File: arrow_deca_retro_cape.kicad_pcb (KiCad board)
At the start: 2 copper layers, 100 x 100 mm, 78 parts, among them J1 DB15_Female_HighDensity_Mount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, J10 Conn_02x06_Odd_Even, J11 PMOD1, J12 PMOD2, J14 Conn_01x02, J15 Conn_01x03, J16 Conn_01x06, J17 Conn_01x02, J18 Conn_01x03, J19 DINC_MIN_TM_6_1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

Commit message: v0.71 gerbers sent for manufacturing
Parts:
- C18: value 10uF -> 1uF
- C19, C21: value 100uF -> 10uF
- C20: value 10uF -> 0.1uF
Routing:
- net GND: track 51.3 -> 61.3 mm, vias 6 -> 7
- net +3V3: track 244.5 -> 253.2 mm, vias 2 -> 3
- net Net-(D5-Pad3): track 137.0 -> 139.6 mm
- net +5V: track 281.3 -> 280.2 mm
- net /MUX: track 84.1 -> 83.6 mm
- net /RX+: track 107.4 -> 107.9 mm
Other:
- board text added: "0.1270 mm / 0.1270 mm"
- board text added: "0.3000 mm"
- board text added: "1.6000 mm"
- board text removed: "0.1270 mm"
- board text removed: "0.1270 mm / 0.0000 mm"
- board text removed: "0.5700 mm"

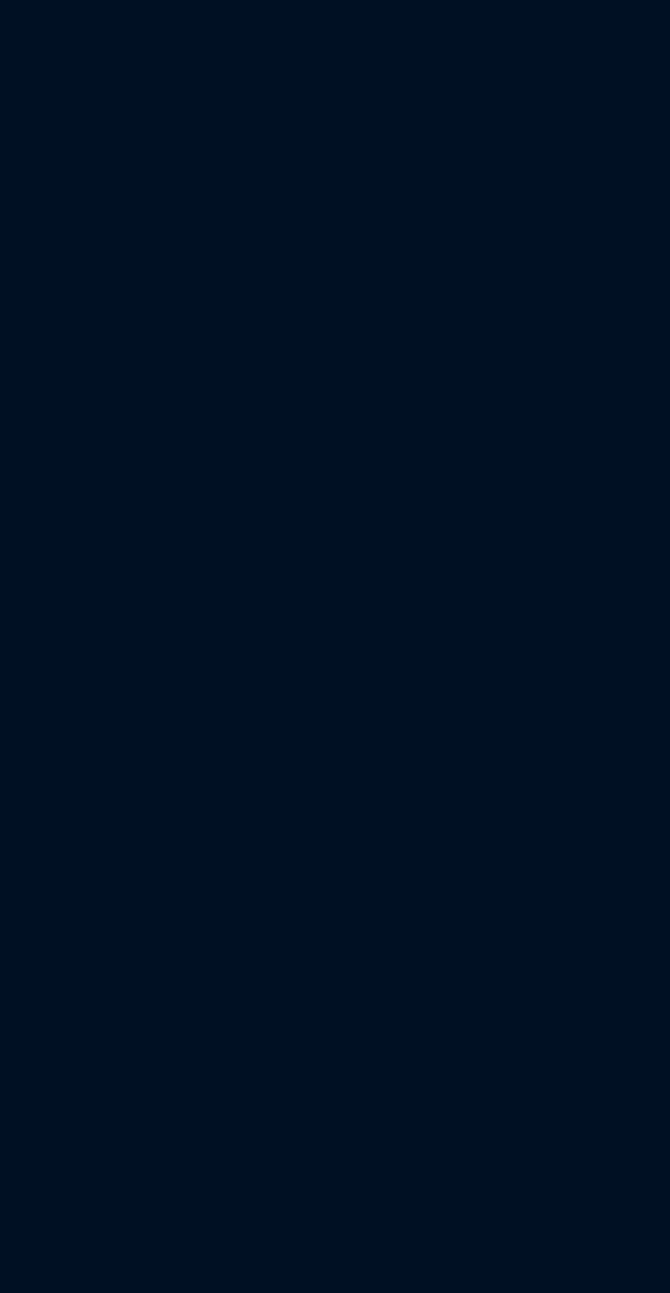
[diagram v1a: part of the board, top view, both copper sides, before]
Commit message: updated status. received pcb. started testing
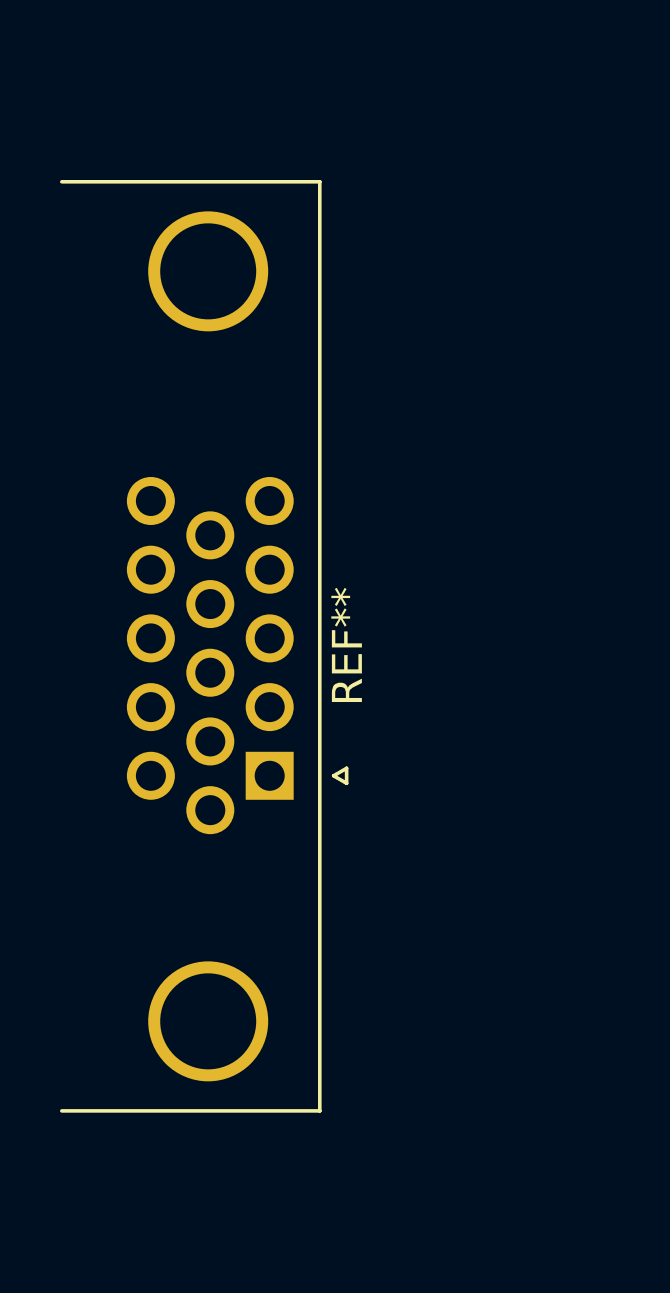
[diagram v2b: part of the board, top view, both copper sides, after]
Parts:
- added REF**: DSUB-15-HD_Female_Horizontal_P2.29x1.98mm_EdgePinOffset3.03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, Connector_Dsub:DSUB-15-HD_Female_Horizontal_P2.29x1.98mm_EdgePinOffset3.03mm_Housed_MountingHolesOffset4.94mm, F.Cu at (53.3, 64.4)
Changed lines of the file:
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@@
     )
   )
-  (property "VERSION" "0.71")
+  (property "VERSION" "0.72")
   (net 0 "")
   (net 1 "GND")
@@
       (offset (xyz 0 0 0))
       (scale (xyz 1 1 1))
+      (rotate (xyz 0 0 0))
+    )
+  )
+  (footprint "Connector_Dsub:DSUB-15-HD_Female_Horizontal_P2.29x1.98mm_EdgePinOffset3.03mm_Housed_MountingHolesOffset4.94mm" (layer "F.Cu")
+    (at 53.34 64.4386 -90)
+    (descr "15-pin D-Sub connector, horizontal/angled (90 deg), THT-mount, female, pitch 2.29x1.98mm, pin-PCB-offset 3.0300000000000002mm, distance of mounting holes 25mm, distance of mounting holes to PCB edge 4.9399999999999995mm, see https://disti-assets.s3.amazonaws.com/tonar/files/datasheets/16730.pdf")
+    (tags "15-pin D-Sub connector horizontal angled 90deg THT female pitch 2.29x1.98mm pin-PCB-offset 3.0300000000000002mm mounting-holes-distance 25mm mounting-hole-offset 25mm")
+    (attr through_hole)
+    (fp_text reference "REF**" (at -4.315 -2.61 90) (layer "F.SilkS")
+      (effects (font (size 1 1) (thickness 0.15)))
+    )
+    (fp_text value "DSUB-15-HD_Female_Horizontal_P2.29x1.98mm_EdgePinOffset3.03mm_Housed_MountingHolesOffset4.94mm" (at -4.315 14.89 90) (layer "F.Fab")
+      (effects (font (size 1 1) (thickness 0.15)))
+    )
+    (fp_text user "${REFERENCE}" (at -4.315 10.39 90) (layer "F.Fab")
+      (effects (font (size 1 1) (thickness 0.15)))
+    )
+    (fp_line (start 0.25 -2.564338) (end 0 -2.131325) (layer "F.SilkS") (width 0.12))
+    (fp_line (start -19.8 -1.67) (end 11.17 -1.67) (layer "F.SilkS") (width 0.12))
+    (fp_line (start -19.8 6.93) (end -19.8 -1.67) (layer "F.SilkS") (width 0.12))
+    (fp_line (start 11.17 -1.67) (end 11.17 6.93) (layer "F.SilkS") (width 0.12))
+    (fp_line (start 0 -2.131325) (end -0.25 -2.564338) (layer "F.SilkS") (width 0.12))
+    (fp_line (start -0.25 -2.564338) (end 0.25 -2.564338) (layer "F.SilkS") (width 0.12))
+    (fp_line (start -20.25 -2.15) (end -20.25 13.9) (layer "F.CrtYd") (width 0.05))
+    (fp_line (start 11.65 13.9) (end 11.65 -2.15) (layer "F.CrtYd") (width 0.05))
+    (fp_line (start -20.25 13.9) (end 11.65 13.9) (layer "F.CrtYd") (width 0.05))
+    (fp_line (start 11.65 -2.15) (end -20.25 -2.15) (layer "F.CrtYd") (width 0.05))
+    (fp_line (start -19.74 6.99) (end 11.11 6.99) (layer "F.Fab") (width 0.1))
+    (fp_line (start -15.215 6.99) (end -15.215 2.05) (layer "F.Fab") (width 0.1))
+    (fp_line (start 10.685 7.39) (end 5.685 7.39) (layer "F.Fab") (width 0.1))
+    (fp_line (start 3.835 13.39) (end 3.835 7.39) (layer "F.Fab") (width 0.1))
+    (fp_line (start -18.415 6.99) (end -18.415 2.05) (layer "F.Fab") (width 0.1))
+    (fp_line (start 10.685 12.39) (end 10.685 7.39) (layer "F.Fab") (width 0.1))
+    (fp_line (start 9.785 6.99) (end 9.785 2.05) (layer "F.Fab") (width 0.1))
+    (fp_line (start -12.465 7.39) (end -12.465 13.39) (layer "F.Fab") (width 0.1))
+    (fp_line (start -19.315 12.39) (end -14.315 12.39) (layer "F.Fab") (width 0.1))
+    (fp_line (start 5.685 7.39) (end 5.685 12.39) (layer "F.Fab") (width 0.1))
+    (fp_line (start -12.465 13.39) (end 3.835 13.39) (layer "F.Fab") (width 0.1))
+    (fp_line (start 11.11 -1.61) (end -19.74 -1.61) (layer "F.Fab") (width 0.1))
+    (fp_line (start -14.315 7.39) (end -19.315 7.39) (layer "F.Fab") (width 0.1))
+    (fp_line (start -19.315 7.39) (end -19.315 12.39) (layer "F.Fab") (width 0.1))
+    (fp_line (start 5.685 12.39) (end 10.685 12.39) (layer "F.Fab") (width 0.1))
+    (fp_line (start -14.315 12.39) (end -14.315 7.39) (layer "F.Fab") (width 0.1))
+    (fp_line (start -19.74 7.39) (end 11.11 7.39) (layer "F.Fab") (width 0.1))
+    (fp_line (start 11.11 6.99) (end 11.11 -1.61) (layer "F.Fab") (width 0.1))
+    (fp_line (start 3.835 7.39) (end -12.465 7.39) (layer "F.Fab") (width 0.1))
+    (fp_line (start 11.11 7.39) (end 11.11 6.99) (layer "F.Fab") (width 0.1))
+    (fp_line (start 11.11 6.99) (end -19.74 6.99) (layer "F.Fab") (width 0.1))
+    (fp_line (start -19.74 -1.61) (end -19.74 6.99) (layer "F.Fab") (width 0.1))
+    (fp_line (start -19.74 6.99) (end -19.74 7.39) (layer "F.Fab") (width 0.1))
+    (fp_line (start 6.585 6.99) (end 6.585 2.05) (layer "F.Fab") (width 0.1))
+    (fp_arc (start -18.415 2.05) (mid -16.815 0.45) (end -15.215 2.05) (layer "F.Fab") (width 0.1))
+    (fp_arc (start 6.585 2.05) (mid 8.185 0.45) (end 9.785 2.05) (layer "F.Fab") (width 0.1))
+    (pad "0" thru_hole circle (at 8.185 2.05 270) (size 4 4) (drill 3.2) (layers *.Cu *.Mask))
+    (pad "0" thru_hole circle (at -16.815 2.05 270) (size 4 4) (drill 3.2) (layers *.Cu *.Mask))
+    (pad "1" thru_hole rect (at 0 0 270) (size 1.6 1.6) (drill 1) (layers *.Cu *.Mask))
+    (pad "2" thru_hole circle (at -2.29 0 270) (size 1.6 1.6) (drill 1) (layers *.Cu *.Mask))
+    (pad "3" thru_hole circle (at -4.58 0 270) (size 1.6 1.6) (drill 1) (layers *.Cu *.Mask))
+    (pad "4" thru_hole circle (at -6.87 0 270) (size 1.6 1.6) (drill 1) (layers *.Cu *.Mask))
+    (pad "5" thru_hole circle (at -9.16 0 270) (size 1.6 1.6) (drill 1) (layers *.Cu *.Mask))
+    (pad "6" thru_hole circle (at 1.145 1.98 270) (size 1.6 1.6) (drill 1) (layers *.Cu *.Mask))
+    (pad "7" thru_hole circle (at -1.145 1.98 270) (size 1.6 1.6) (drill 1) (layers *.Cu *.Mask))
+    (pad "8" thru_hole circle (at -3.435 1.98 270) (size 1.6 1.6) (drill 1) (layers *.Cu *.Mask))
+    (pad "9" thru_hole circle (at -5.725 1.98 270) (size 1.6 1.6) (drill 1) (layers *.Cu *.Mask))
+    (pad "10" thru_hole circle (at -8.015 1.98 270) (size 1.6 1.6) (drill 1) (layers *.Cu *.Mask))
+    (pad "11" thru_hole circle (at 0 3.96 270) (size 1.6 1.6) (drill 1) (layers *.Cu *.Mask))
+    (pad "12" thru_hole circle (at -2.29 3.96 270) (size 1.6 1.6) (drill 1) (layers *.Cu *.Mask))
+    (pad "13" thru_hole circle (at -4.58 3.96 270) (size 1.6 1.6) (drill 1) (layers *.Cu *.Mask))
+    (pad "14" thru_hole circle (at -6.87 3.96 270) (size 1.6 1.6) (drill 1) (layers *.Cu *.Mask))
+    (pad "15" thru_hole circle (at -9.16 3.96 270) (size 1.6 1.6) (drill 1) (layers *.Cu *.Mask))
+    (model "${KICAD6_3DMODEL_DIR}/Connector_Dsub.3dshapes/DSUB-15-HD_Female_Horizontal_P2.29x1.98mm_EdgePinOffset3.03mm_Housed_MountingHolesOffset4.94mm.wrl"
+      (offset (xyz 0 0 0))
+      (scale (xyz 1 1 1))

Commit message: v0.75 see changelog
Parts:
- removed J3: Conn_01x06, Connector_PinHeader_2.54mm:PinHeader_1x06_P2.54mm_Vertical
- removed REF**: DSUB-15-HD_Female_Horizontal_P2.29x1.98mm_EdgePinOffset3.03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, Connector_Dsub:DSUB-15-HD_Female_Horizontal_P2.29x1.98mm_EdgePinOffset3.03mm_Housed_MountingHolesOffset4.94mm
- added JP3: SolderJumper_2_Open, Jumper:SolderJumper-2_P1.3mm_Open_RoundedPad1.0x1.5mm, B.Cu at (165.1, 126.6)
- added JP4: Conn_01x02, Connector_PinHeader_2.54mm:PinHeader_1x02_P2.54mm_Vertical, F.Cu at (113.0, 48.3)
- D1, D12, D2, D3, D4: value BAT54S -> MMSZ5225BG; footprint Package_TO_SOT_SMD:SOT-23 -> Diode_SMD:D_SOD-123
- D10, D11, D5, D6, D7, D8, D9: value BAT54S -> MMSZ5221BT1G; footprint Package_TO_SOT_SMD:SOT-23 -> Diode_SMD:D_SOD-123
- J1: footprint vga:DSUB-15-HD_Female_Horizontal_P2.29x2.54mm_EdgePinOffset3.03mm_Housed_MountingHolesOffset4.94mm -> Connector_Dsub:DSUB-15-HD_Female_Horizontal_P2.29x1.98mm_EdgePinOffset3.03mm_Housed_MountingHolesOffset4.94mm
- J10: footprint Connector_PinSocket_2.54mm:PinSocket_2x06_P2.54mm_Vertical -> Connector_PinSocket_2.54mm:PinSocket_1x06_P2.54mm_Vertical
- J16: footprint Connector_PinHeader_2.54mm:PinHeader_1x06_P2.54mm_Vertical -> Connector_PinSocket_2.54mm:PinSocket_1x06_P2.54mm_Vertical
- LO2: value OSHW-Logo2_9.8x8mm_SilkScreen -> OSHW-Logo2_14.6x12mm_SilkScreen; footprint Symbol:OSHW-Logo2_9.8x8mm_SilkScreen -> Symbol:OSHW-Logo2_14.6x12mm_SilkScreen
- R1, R10, R11, R12, R13, R14, R15, R16, R2, R5, R6, R9: value 180 -> 510
- R3, R4: value DNI -> DNI 4k7
- moved D2 75.8 mm to (197.7, 94.0)
- moved D1 75.5 mm to (203.5, 90.7)
- moved D4 67.5 mm to (209.2, 90.7)
- moved D12 64.4 mm to (203.5, 87.3), turned to 0 degrees
- moved D5 62.7 mm to (215.0, 87.3), turned to 0 degrees
- moved D7 62.5 mm to (209.2, 94.0), turned to 0 degrees
- moved D6 56.5 mm to (197.7, 90.7), turned to 0 degrees
- moved D8 55.4 mm to (203.5, 97.4), turned to 0 degrees
- moved D10 53.5 mm to (209.2, 87.3), turned to 0 degrees
- moved D3 52.2 mm to (197.7, 87.3)
- moved D9 44.9 mm to (197.7, 97.4), turned to 0 degrees
- moved D11 44.3 mm to (203.5, 94.0), turned to 0 degrees
- moved LO2 0.95 mm to (106.3, 115.9)
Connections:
- net /JOY_MUX_DETO3 renamed /DETO3_JOY_MUX
- net /SPI_CS_FPGA renamed /SPI_CS2
- net /SPI_CS_IO renamed /SPI_CS1
- net /SPI_CS_OSD renamed /SPI_CS0_CLKBD
- net /SPI_DI (MISO) renamed /SPI_MISO_WSDB
- net /SPI_DO (MOSI) renamed /SPI_MOSI
- net /SPI_SCK renamed /SPI_SCLK_DABD
- D1 pad 1: GND -> /PS2_KEYB_CLK
- D1 pad 2: +3V3 -> GND
- D10 pad 1: GND -> /JOY1_UP
- D10 pad 2: +2V5 -> GND
- D11 pad 1: GND -> unconnected-(D11-Pad1)
- D11 pad 2: +2V5 -> GND
- D12 pad 1: GND -> unconnected-(D12-Pad1)
- D12 pad 2: +2V5 -> GND
- D2 pad 1: GND -> /PS2_KEYB_DAT
- D2 pad 2: +3V3 -> GND
- D3 pad 1: GND -> /PS2_MOUSE_CLK
- D3 pad 2: +3V3 -> GND
- D4 pad 1: GND -> /PS2_MOUSE_DAT
- D4 pad 2: +3V3 -> GND
- D5 pad 1: GND -> /JOY1_B2_P9
- D5 pad 2: +2V5 -> GND
- D6 pad 1: GND -> /JOY1_DOWN
- D6 pad 2: +2V5 -> GND
- D7 pad 1: GND -> /JOY1_RIGHT
- D7 pad 2: +2V5 -> GND
- D8 pad 1: GND -> /JOY1_B1_P6
- D8 pad 2: +2V5 -> GND
- D9 pad 1: GND -> /JOY1_LEFT
- D9 pad 2: +2V5 -> GND
- J1 pad 9: unconnected-(J1-Pad9) -> Net-(JP4-Pad1)
- J10 pad 2: +2V5 -> +5V
- J10 pad 3: +5V -> GND
- J10 pad 4: +5V -> +3.3VP
- J10 pad 5: +3.3VP -> GND
- J10 pad 6: +3.3VP -> /3V3_LDO
- J19 pad 1: Net-(D3-Pad3) -> Net-(J19-Pad1)
- J19 pad 5: Net-(D4-Pad3) -> Net-(J19-Pad5)
- J22 pad 1: Net-(D5-Pad3) -> Net-(J22-Pad1)
- J4 pad 9: Net-(D5-Pad3) -> Net-(J22-Pad1)
- J5 pad 1: Net-(D1-Pad3) -> Net-(J5-Pad1)
- J5 pad 5: Net-(D2-Pad3) -> Net-(J5-Pad5)
- R1 pad 2: Net-(D2-Pad3) -> Net-(J5-Pad5)
- R16 pad 2: /MUX -> Net-(JP3-Pad1)
- R2 pad 2: Net-(D1-Pad3) -> Net-(J5-Pad1)
- R3 pad 1: Net-(D1-Pad3) -> Net-(J5-Pad1)
- R4 pad 1: Net-(D2-Pad3) -> Net-(J5-Pad5)
- R5 pad 2: Net-(D4-Pad3) -> Net-(J19-Pad5)
- R6 pad 2: Net-(D3-Pad3) -> Net-(J19-Pad1)
- R9 pad 2: Net-(D5-Pad3) -> Net-(J22-Pad1)
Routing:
- net Net-(J22-Pad1): track 0.00 -> 139.6 mm, vias 0 -> 3
- net Net-(D5-Pad3): track 139.6 -> 0.00 mm, vias 3 -> 0
- net +3V3: track 253.2 -> 197.4 mm
- net +2V5: track 86.5 -> 35.7 mm, vias 9 -> 1
- net Net-(JP3-Pad1): track 0.00 -> 40.8 mm, vias 0 -> 1
- net /MUX: track 83.6 -> 43.5 mm, vias 0 -> 1
- net Net-(JP4-Pad1): track 0.00 -> 29.2 mm
- net Net-(J5-Pad1): track 0.00 -> 19.1 mm
- net Net-(D1-Pad3): track 19.1 -> 0.00 mm
- net Net-(J5-Pad5): track 0.00 -> 16.1 mm
- net Net-(D2-Pad3): track 16.1 -> 0.00 mm
- net Net-(J19-Pad1): track 0.00 -> 14.6 mm
- net Net-(D3-Pad3): track 14.6 -> 0.00 mm
- net Net-(J19-Pad5): track 0.00 -> 13.1 mm
- net Net-(D4-Pad3): track 13.1 -> 0.00 mm
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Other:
- outline, holes or cut-outs redrawn
- board text added: "3V3VP"
- board text added: "JOY_MUX(3)"
- board text removed: "TCK"
- board text removed: "TDI"
- board text removed: "TDO"
- board text removed: "TMS"
- board text removed: "created by Hard Team Deca Somhic & Rhoderik & C.Palmero"

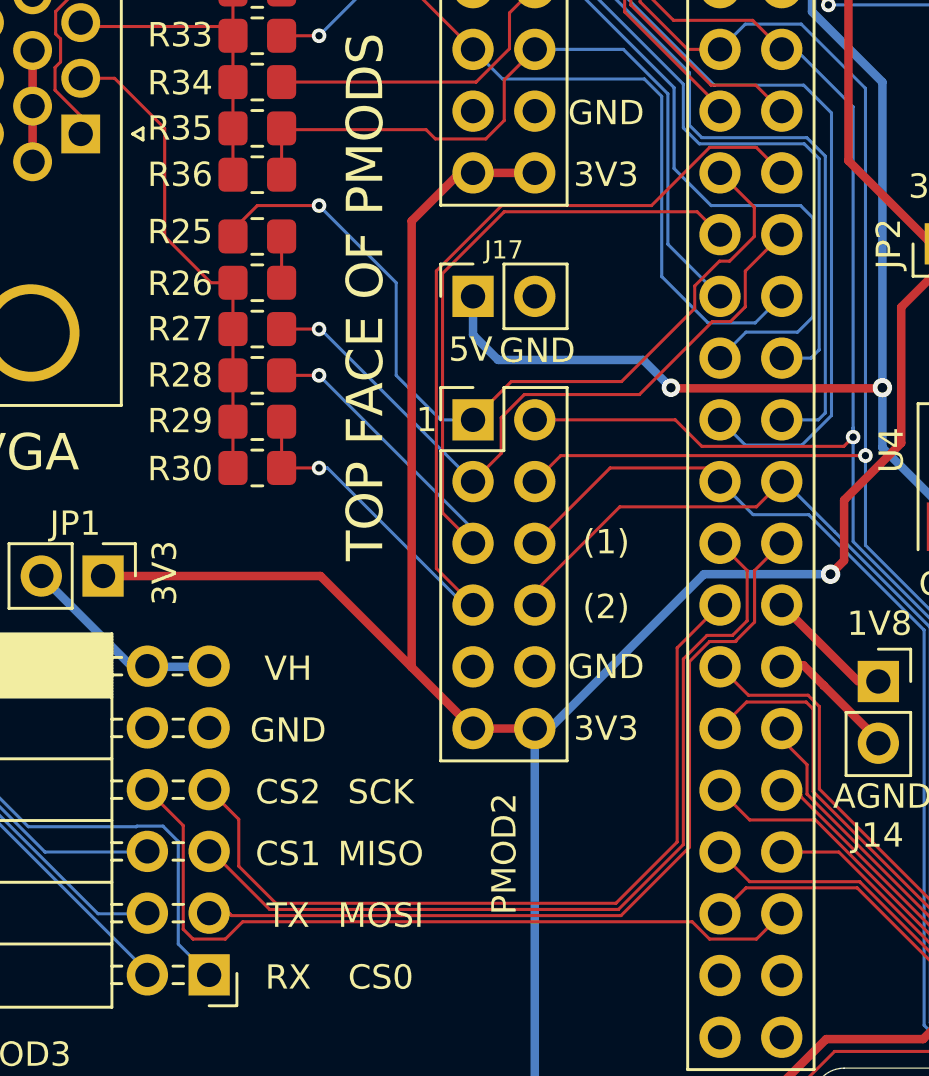
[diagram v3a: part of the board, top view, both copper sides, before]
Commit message: v0.76 double pmod added 4 central pins
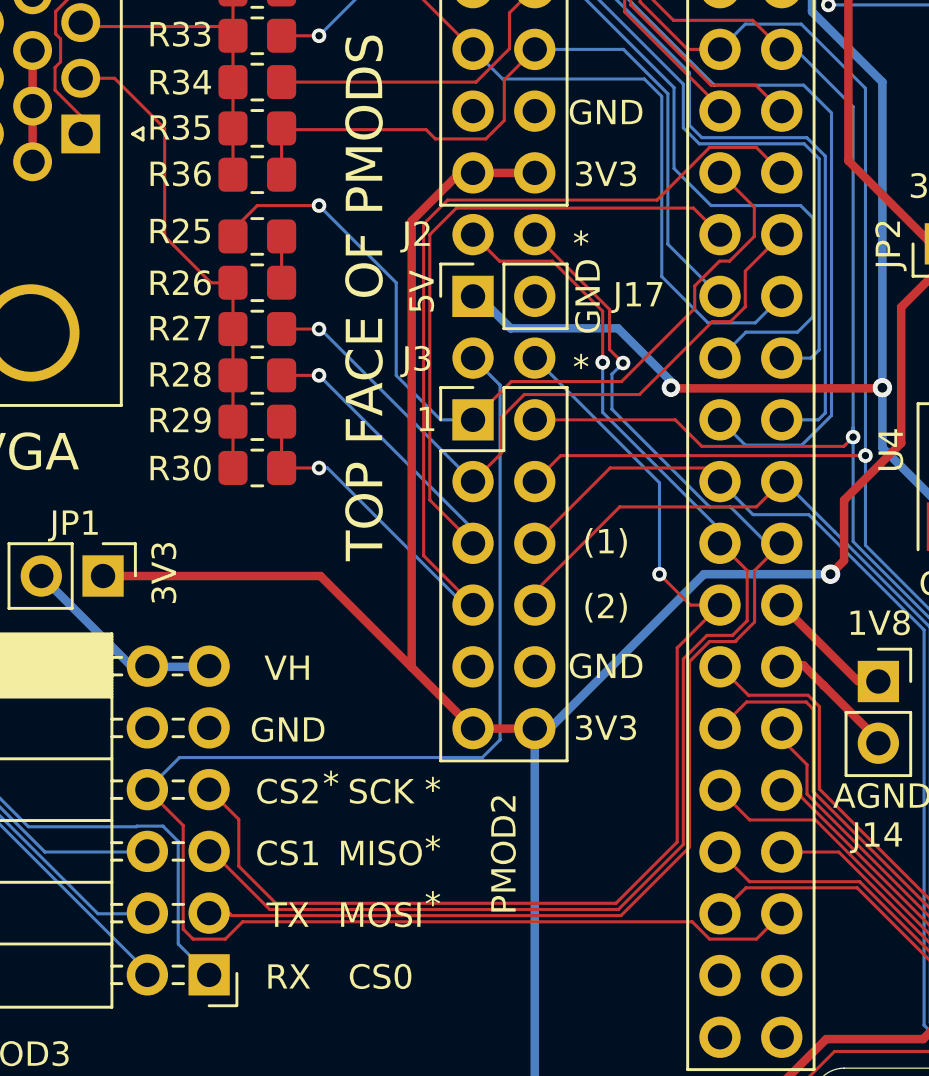
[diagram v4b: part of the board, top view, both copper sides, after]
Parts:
- added J2: Conn_02x01, Connector_PinSocket_2.54mm:PinSocket_1x02_P2.54mm_Vertical, F.Cu at (106.7, 68.6)
- added J3: Conn_02x01, Connector_PinSocket_2.54mm:PinSocket_1x02_P2.54mm_Vertical, F.Cu at (106.7, 73.7)
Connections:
- J12 pad 10: /DETO2 -> unconnected-(J12-Pad10)
- J12 pad 7: /VGA_HS -> unconnected-(J12-Pad7)
- J12 pad 8: /VGA_VS -> unconnected-(J12-Pad8)
- J12 pad 9: /DETO1 -> unconnected-(J12-Pad9)
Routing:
- net /SPI_CS2: track 32.2 -> 63.7 mm
- net /SPI_MISO_WSDB: track 36.2 -> 54.3 mm, vias 0 -> 1
- net /SPI_MOSI: track 35.4 -> 53.6 mm, vias 0 -> 1
- net /SPI_SCLK_DABD: track 33.8 -> 47.9 mm, vias 0 -> 1
- net /VGA_G3: track 43.2 -> 45.1 mm
- net /VGA_G2: track 35.6 -> 37.4 mm
- net +5V: track 281.5 -> 280.7 mm
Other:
- board text added: "*"

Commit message: v0.77 see changelog
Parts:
- added JP5: Conn_01x02, Connector_PinHeader_2.54mm:PinHeader_1x02_P2.54mm_Vertical, F.Cu at (161.2, 62.0)
- added JP6: Conn_01x02, Connector_PinHeader_2.54mm:PinHeader_1x02_P2.54mm_Vertical, F.Cu at (161.2, 85.1)
- added JP7: SolderJumper_3_Open, Jumper:SolderJumper-3_P2.0mm_Open_TrianglePad1.0x1.5mm, F.Cu at (141.2, 88.1)
- JP2: value Conn_01x03 -> SolderJumper_3_Open; footprint Connector_PinHeader_2.54mm:PinHeader_1x03_P2.54mm_Vertical -> Jumper:SolderJumper-3_P2.0mm_Open_TrianglePad1.0x1.5mm
- moved JP2 2.54 mm to (128.7, 69.0), turned to 0 degrees
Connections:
- J10 pad 3: GND -> +3.3VP
- J10 pad 4: +3.3VP -> GND
- J4 pad 5: +5V -> /+JOY_PWR
- J6 pad 11: +5V -> Net-(J6-Pad11)
- J6 pad 29: +3V3 -> Net-(J6-Pad29)
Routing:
- net +5V: track 280.7 -> 210.1 mm, vias 5 -> 4
- net /+JOY_PWR: track 0.00 -> 51.0 mm
- net GND: track 68.4 -> 43.7 mm
- net Net-(J6-Pad11): track 0.00 -> 19.4 mm, vias 0 -> 1
- net Net-(J6-Pad29): track 0.00 -> 17.5 mm, vias 0 -> 1
- net +3V3: track 197.4 -> 180.3 mm, vias 3 -> 2
- net Net-(J5-Pad5): track 16.1 -> 2.81 mm
- net Net-(J19-Pad5): track 13.1 -> 0.00 mm
- net +3.3VP: track 41.1 -> 46.0 mm, vias 0 -> 1
